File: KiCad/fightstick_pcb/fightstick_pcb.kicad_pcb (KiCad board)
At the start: 2 copper layers, 80.5 x 70 mm, 96 parts, among them J1 USB_B_Micro, J2 Conn_01x02, J3 Conn_01x02, J4 Screw_Terminal_01x12, J5 Screw_Terminal_01x12, J6 Screw_Terminal_01x12, SW1 SW_Push, U1 SN74LVC1G14DBV, U10 SN74LVC1G14DBV, U11 SN74LVC1G14DBV, U12 SN74LVC1G14DBV, U13 SN74LVC1G14DBV, U14 SN74LVC1G14DBV, U15 SN74LVC1G14DBV, U2 SN74LVC1G14DBV, U3 NCP1117-3.3_SOT223, U4 W25Q128JVS, U5 SN74LVC1G14DBV, U6 SN74LVC1G14DBV, U7 SN74LVC1G14DBV, U8 SN74LVC1G14DBV, U9 RP2040, Y1 ABM8-272-T3

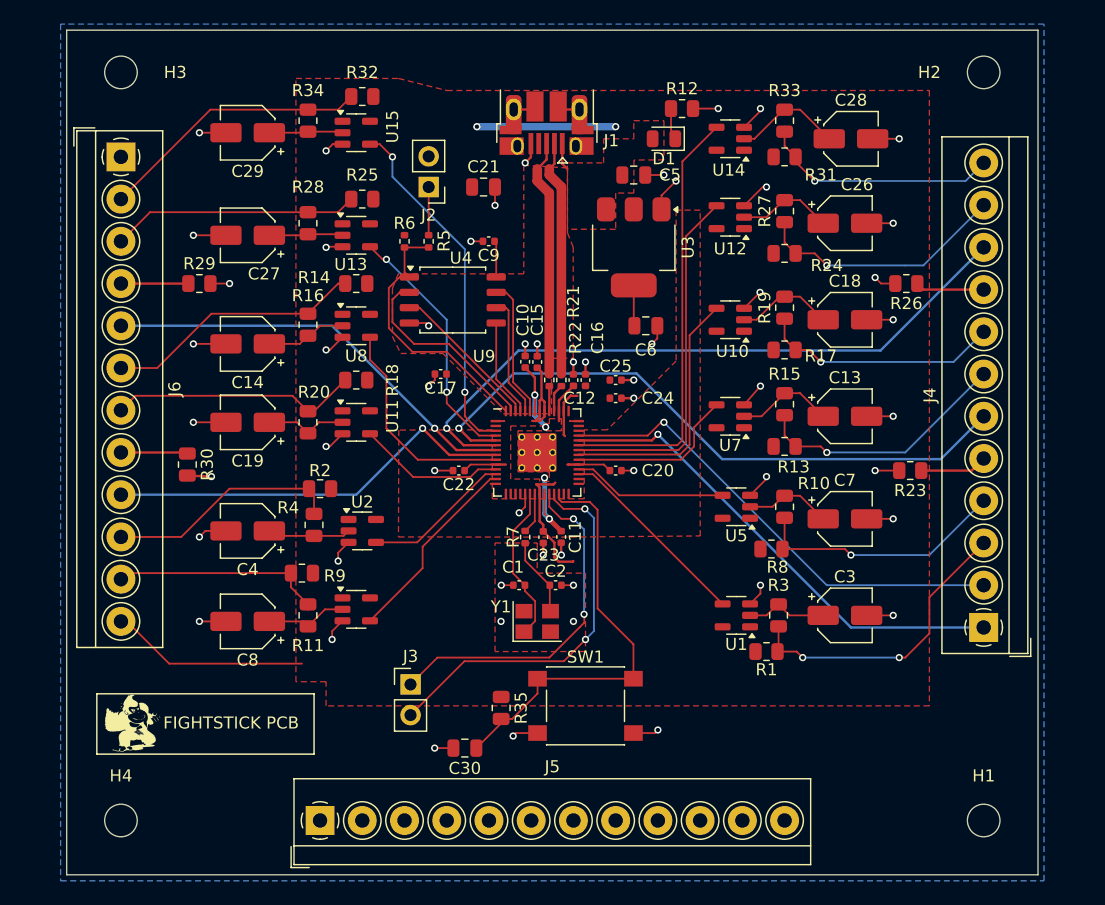
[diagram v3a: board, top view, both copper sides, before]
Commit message: PCB V1.1.0
Améliorations avec cap polarisés
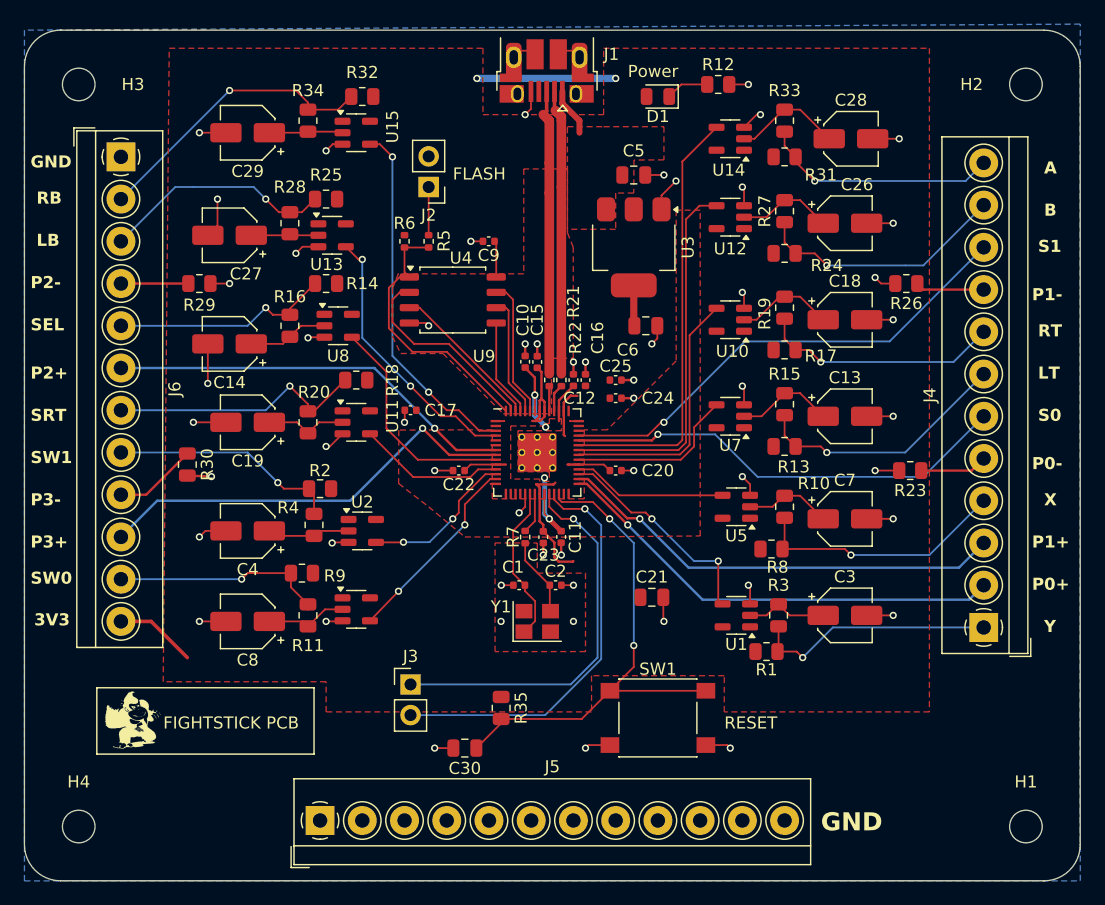
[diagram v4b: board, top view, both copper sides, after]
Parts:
- removed REF**: KiCad-Logo2_5mm_SilkScreen, Symbol:KiCad-Logo2_5mm_SilkScreen
- removed REF**: WEEE-Logo_4.2x6mm_SilkScreen, Symbol:WEEE-Logo_4.2x6mm_SilkScreen
- R12, R23, R26, R29, R30: value 1k -> 130
- R35: value 10k -> 1k
- moved C21 36.8 mm to (109.5, 112.0)
- moved SW1 6.08 mm to (110.0, 122.0)
- moved J1 4.33 mm to (100.8, 67.2)
- moved C17 3.91 mm to (89.5, 96.5)
- moved H2 3.64 mm to (140.5, 69.5)
- moved H3 3.64 mm to (62.0, 69.5)
- moved R12 3.61 mm to (115.0, 69.5)
- moved D1 3.54 mm to (110.0, 70.5)
- moved H1 3.54 mm to (140.5, 131.0)
- moved H4 3.54 mm to (62.0, 131.0)
- moved R25 3.00 mm to (82.5, 79.0)
- moved R14 2.50 mm to (82.5, 86.0)
- moved U13 2.00 mm to (83.0, 82.0)
- moved R16 1.50 mm to (79.5, 89.5)
- moved C14 1.50 mm to (74.5, 91.0)
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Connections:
- D1 pad 2: VBUS -> +3V3
- J4 pad 1: /SIG_STICK_0 -> /SW_Y
- J4 pad 10: /LED_P1+ -> /SIG_STICK_1
- J4 pad 2: /SIG_STICK_1 -> /LED_P0+
- J4 pad 3: /SW_Y -> /LED_P1+
- J4 pad 6: /LED_P0+ -> /SIG_STICK_0
- J6 pad 10: /SW_1 -> /LED_P3+
- J6 pad 5: /LED_P2+ -> /SW_SELECT
- J6 pad 6: /SW_SELECT -> /LED_P2+
- J6 pad 8: /LED_P3- -> /SW_1
- J6 pad 9: /LED_P3+ -> /LED_P3-
- U9 pad 29: unconnected-(U9-GPIO18-Pad29) -> /LED_P0+
- U9 pad 30: unconnected-(U9-GPIO19-Pad30) -> /LED_P1+
- U9 pad 5: /LED_P0+ -> unconnected-(U9-GPIO3-Pad5)
- U9 pad 6: /LED_P1+ -> unconnected-(U9-GPIO4-Pad6)
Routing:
- net /LED_P1+: track 55.6 -> 37.5 mm
- net /LED_P0+: track 53.3 -> 38.8 mm
- net +3V3: track 64.9 -> 55.7 mm
- net /RUN: track 35.6 -> 42.4 mm, vias 0 -> 2
- net /SW_Y: track 25.1 -> 20.5 mm, vias 2 -> 1
- net /USB_D+: track 19.8 -> 23.7 mm
- net /USB_D-: track 19.7 -> 23.5 mm
- net Net-(J3-Pin_1): track 29.0 -> 32.2 mm, vias 2 -> 1
- net /SW_SELECT: track 21.5 -> 18.3 mm, vias 0 -> 1
- net /SIG_STICK_0: track 40.4 -> 37.3 mm
- net GND: track 98.2 -> 95.8 mm
- net Net-(J3-Pin_2): track 32.4 -> 34.6 mm, vias 2 -> 1
- net /SIG_Y: track 16.4 -> 18.2 mm, vias 0 -> 2
- net /SIG_LB: track 21.0 -> 22.7 mm
- net VBUS: track 2.28 -> 4.01 mm
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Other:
- board size 80.5 x 70 mm -> 87.5 x 70.5 mm
- board text added: "3V3"
- board text added: "A"
- board text added: "B"
- board text added: "FLASH"
- board text added: "GND"
- board text added: "LB"
- board text added: "LT"
- board text added: "P0+"
- board text added: "P0-"
- board text added: "P1+"
- board text added: "P1-"
- board text added: "P2+"
- board text added: "P2-"
- board text added: "P3+"
- board text added: "P3-"
- board text added: "Power"
- board text added: "RB"
- board text added: "RESET"
- board text added: "RT"
- board text added: "S0"
- board text added: "S1"
- board text added: "SEL"
- board text added: "SRT"
- board text added: "SW0"
- board text added: "SW1"
- board text added: "X"
- board text added: "Y"

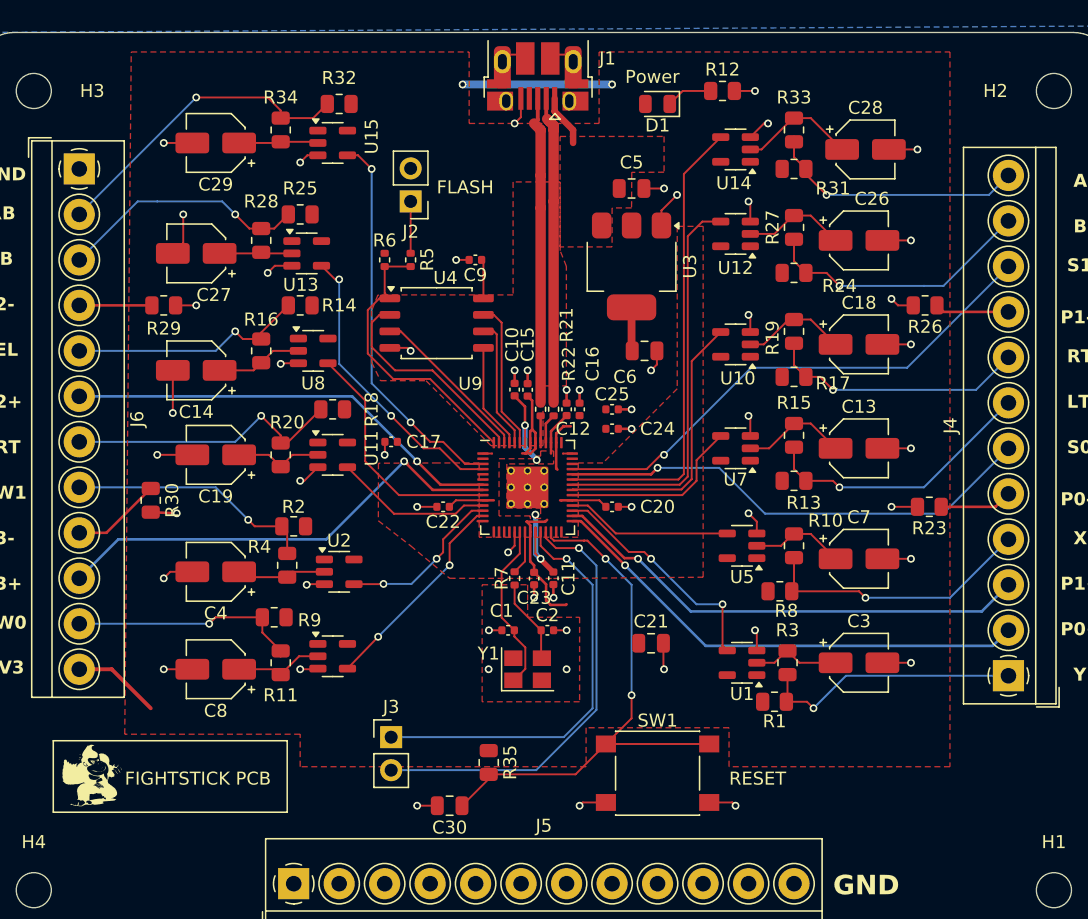
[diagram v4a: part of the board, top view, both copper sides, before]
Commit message: PCB V1.2
Il n'y a plus de condensateurs polarisés
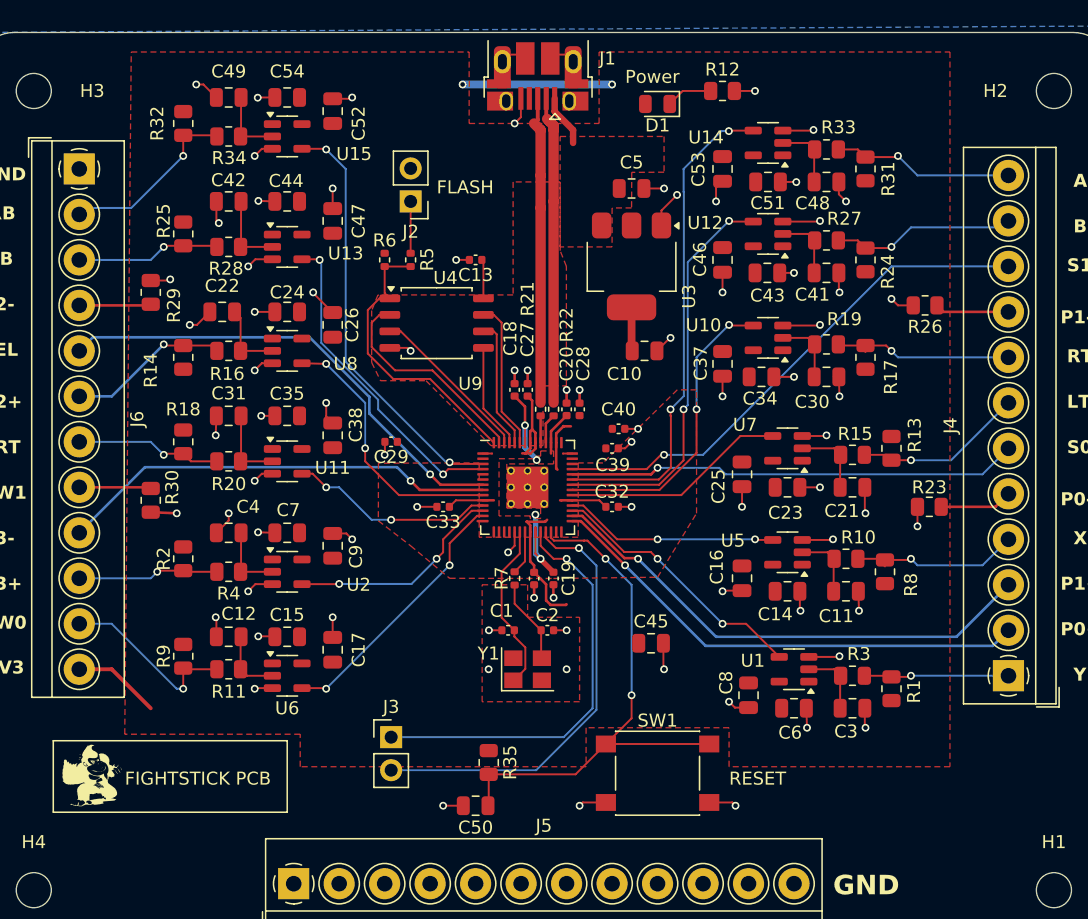
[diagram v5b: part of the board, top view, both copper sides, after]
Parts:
- added C31: 1u, Capacitor_SMD:C_0805_2012Metric, F.Cu at (77.0, 94.5)
- added C32: 100n, Capacitor_SMD:C_0402_1005Metric, F.Cu at (106.5, 101.5)
- added C33: 100n, Capacitor_SMD:C_0402_1005Metric, F.Cu at (93.5, 101.5)
- added C34: 0.1u, Capacitor_SMD:C_0805_2012Metric, F.Cu at (118.0, 91.5)
- added C35: 0.1u, Capacitor_SMD:C_0805_2012Metric, F.Cu at (81.5, 94.5)
- added C36: 100n, Capacitor_SMD:C_0402_1005Metric, F.Cu at (100.5, 107.0)
- added C37: 1u, Capacitor_SMD:C_0805_2012Metric, F.Cu at (115.0, 90.5)
- added C38: 1u, Capacitor_SMD:C_0805_2012Metric, F.Cu at (85.0, 96.0)
- added C39: 100n, Capacitor_SMD:C_0402_1005Metric, F.Cu at (106.5, 97.0)
- added C40: 100n, Capacitor_SMD:C_0402_1005Metric, F.Cu at (107.0, 95.5)
- added C41: 1u, Capacitor_SMD:C_0805_2012Metric, F.Cu at (123.0, 83.5)
- added C42: 1u, Capacitor_SMD:C_0805_2012Metric, F.Cu at (77.0, 78.0)
- added C43: 0.1u, Capacitor_SMD:C_0805_2012Metric, F.Cu at (118.5, 83.5)
- added C44: 0.1u, Capacitor_SMD:C_0805_2012Metric, F.Cu at (81.5, 78.0)
- added C45: 10u, Capacitor_SMD:C_0805_2012Metric, F.Cu at (109.5, 112.0)
- added C46: 1u, Capacitor_SMD:C_0805_2012Metric, F.Cu at (115.0, 82.5)
- added C47: 1u, Capacitor_SMD:C_0805_2012Metric, F.Cu at (85.0, 79.5)
- added C48: 1u, Capacitor_SMD:C_0805_2012Metric, F.Cu at (123.0, 76.5)
- added C49: 1u, Capacitor_SMD:C_0805_2012Metric, F.Cu at (77.0, 70.0)
- added C50: 100n, Capacitor_SMD:C_0805_2012Metric, F.Cu at (96.0, 124.5)
- added C51: 0.1u, Capacitor_SMD:C_0805_2012Metric, F.Cu at (118.5, 76.5)
- added C52: 0.1u, Capacitor_SMD:C_0805_2012Metric, F.Cu at (85.0, 71.0)
- added C53: 1u, Capacitor_SMD:C_0805_2012Metric, F.Cu at (115.0, 75.5)
- added C54: 1u, Capacitor_SMD:C_0805_2012Metric, F.Cu at (81.5, 70.0)
- C10: value 100n -> 10u; footprint Capacitor_SMD:C_0402_1005Metric -> Capacitor_SMD:C_0805_2012Metric
- C11, C17, C22, C25, C9: value 100n -> 1u; footprint Capacitor_SMD:C_0402_1005Metric -> Capacitor_SMD:C_0805_2012Metric
- C12, C16: footprint Capacitor_SMD:C_0402_1005Metric -> Capacitor_SMD:C_0805_2012Metric
- C13, C18, C19, C27, C29: value 1u -> 100n; footprint Capacitor_SMD:CP_Elec_4x3 -> Capacitor_SMD:C_0402_1005Metric
- C14, C7: value 1u -> 0.1u; footprint Capacitor_SMD:CP_Elec_4x3 -> Capacitor_SMD:C_0805_2012Metric
- C15, C23, C24: value 100n -> 0.1u; footprint Capacitor_SMD:C_0402_1005Metric -> Capacitor_SMD:C_0805_2012Metric
- C20, C30: value 100n -> 1u
- C21: value 10u -> 1u
- C26, C3, C4, C8: footprint Capacitor_SMD:CP_Elec_4x3 -> Capacitor_SMD:C_0805_2012Metric
- C28: footprint Capacitor_SMD:CP_Elec_4x3 -> Capacitor_SMD:C_0402_1005Metric
- C6: value 10u -> 0.1u
- moved C14 48.6 mm to (120.0, 108.0), turned to 0 degrees
- moved C7 44.0 mm to (81.5, 103.5), turned to 180 degrees
- moved C30 43.9 mm to (123.0, 91.5), turned to 0 degrees
- moved C8 41.0 mm to (117.0, 116.0), turned to -90 degrees
- moved C26 41.0 mm to (85.0, 87.5), turned to 90 degrees
- moved C13 32.9 mm to (96.0, 82.5), turned to 180 degrees
- moved C12 31.3 mm to (77.0, 111.5), turned to 180 degrees
- moved C6 29.8 mm to (120.5, 117.0)
- moved C28 29.7 mm to (104.0, 94.0), turned to 90 degrees
- moved C19 27.7 mm to (102.0, 107.0), turned to -90 degrees
- moved C27 27.6 mm to (100.0, 92.5), turned to 90 degrees
- moved C18 26.7 mm to (99.0, 92.5), turned to 90 degrees
- moved C29 26.7 mm to (89.5, 96.5)
- moved C24 26.6 mm to (81.5, 86.5), turned to 180 degrees
- moved C15 26.5 mm to (81.5, 111.5), turned to 180 degrees
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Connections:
- C10 pad 1: +1V1 -> +3V3
- C11 pad 1: +1V1 -> Net-(C11-Pad1)
- C12 pad 1: +1V1 -> Net-(C12-Pad1)
- C13 pad 1: Net-(C13-Pad1) -> +3V3
- C14 pad 1: Net-(C14-Pad1) -> +3V3
- C18 pad 1: Net-(C18-Pad1) -> +1V1
- C19 pad 1: Net-(C19-Pad1) -> +1V1
- C20 pad 1: +3V3 -> +1V1
- C21 pad 1: +3V3 -> Net-(C21-Pad1)
- C22 pad 1: +3V3 -> Net-(C22-Pad1)
- C26 pad 1: Net-(C26-Pad1) -> +3V3
- C27 pad 1: Net-(C27-Pad1) -> +3V3
- C28 pad 1: Net-(C28-Pad1) -> +3V3
- C29 pad 1: Net-(C29-Pad1) -> +3V3
- C30 pad 1: /RUN -> Net-(C30-Pad1)
- C7 pad 1: Net-(C7-Pad1) -> +3V3
- C8 pad 1: Net-(C8-Pad1) -> +3V3
- J6 pad 10: /LED_P3+ -> /SW_1
- J6 pad 5: /SW_SELECT -> /LED_P2+
- J6 pad 6: /LED_P2+ -> /SW_SELECT
- J6 pad 8: /SW_1 -> /LED_P3-
- J6 pad 9: /LED_P3- -> /LED_P3+
- R10 pad 2: Net-(C7-Pad1) -> Net-(C11-Pad1)
- R11 pad 2: Net-(C8-Pad1) -> Net-(C12-Pad1)
- R15 pad 2: Net-(C13-Pad1) -> Net-(C21-Pad1)
- R16 pad 2: Net-(C14-Pad1) -> Net-(C22-Pad1)
- R19 pad 2: Net-(C18-Pad1) -> Net-(C30-Pad1)
- R20 pad 2: Net-(C19-Pad1) -> Net-(C31-Pad1)
- R27 pad 2: Net-(C26-Pad1) -> Net-(C41-Pad1)
- R28 pad 2: Net-(C27-Pad1) -> Net-(C42-Pad1)
- R33 pad 2: Net-(C28-Pad1) -> Net-(C48-Pad1)
- R34 pad 2: Net-(C29-Pad1) -> Net-(C49-Pad1)
- U10 pad 2: Net-(C18-Pad1) -> Net-(C30-Pad1)
- U11 pad 2: Net-(C19-Pad1) -> Net-(C31-Pad1)
- U12 pad 2: Net-(C26-Pad1) -> Net-(C41-Pad1)
- U13 pad 2: Net-(C27-Pad1) -> Net-(C42-Pad1)
- U14 pad 2: Net-(C28-Pad1) -> Net-(C48-Pad1)
- U15 pad 2: Net-(C29-Pad1) -> Net-(C49-Pad1)
- U5 pad 2: Net-(C7-Pad1) -> Net-(C11-Pad1)
- U6 pad 2: Net-(C8-Pad1) -> Net-(C12-Pad1)
- U7 pad 2: Net-(C13-Pad1) -> Net-(C21-Pad1)
- U8 pad 2: Net-(C14-Pad1) -> Net-(C22-Pad1)
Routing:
- net GND: track 95.8 -> 129.4 mm, vias 55 -> 79
- net /SW_START: track 21.7 -> 11.3 mm
- net /SW_RB: track 24.3 -> 14.1 mm
- net /SW_Y: track 20.5 -> 11.3 mm
- net Net-(C28-Pad1): track 9.06 -> 0.00 mm
- net Net-(C18-Pad1): track 8.67 -> 0.00 mm
- net /SW_X: track 21.4 -> 12.8 mm
- net /SW_1: track 19.1 -> 10.9 mm
- net Net-(C13-Pad1): track 8.15 -> 0.00 mm
- net /SW_LT: track 21.5 -> 13.3 mm
- net Net-(C26-Pad1): track 7.94 -> 0.00 mm
- net /SW_LB: track 19.3 -> 11.6 mm
- net /SW_B: track 21.6 -> 14.2 mm
- net Net-(C7-Pad1): track 7.23 -> 0.00 mm
- net Net-(C8-Pad1): track 6.82 -> 0.00 mm
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
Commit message: PCB V1.2.1
Tous les condensateurs et résistances sont maintenant plus gros
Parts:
- C1, C13, C18, C19, C2, C20, C27, C28, C29, C32, C33, C36, C39, C40: footprint Capacitor_SMD:C_0402_1005Metric -> Capacitor_SMD:C_0805_2012Metric
- R21, R22, R5, R6, R7: footprint Resistor_SMD:R_0402_1005Metric -> Resistor_SMD:R_0805_2012Metric
- moved C13 7.52 mm to (95.5, 75.0)
- moved R5 5.10 mm to (92.0, 77.5)
- moved R6 5.00 mm to (89.0, 77.5)
- moved U4 4.86 mm to (93.0, 82.5)
- moved J2 4.72 mm to (91.0, 73.3)
- moved C18 4.47 mm to (97.0, 88.5)
- moved C27 4.12 mm to (99.0, 88.5)
- moved J3 3.00 mm to (86.5, 119.2)
- moved R21 2.11 mm to (99.5, 92.5)
- moved C28 1.80 mm to (105.5, 93.0)
- moved C40 1.80 mm to (108.5, 94.5)
- moved Y1 1.80 mm to (98.5, 115.0)
- moved R22 1.57 mm to (101.5, 92.5)
- moved C19 1.51 mm to (103.5, 107.0)
- moved C1 1.50 mm to (97.0, 111.0)
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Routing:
- net +3V3: track 55.7 -> 69.0 mm
- net /QSPI_SD3: track 11.5 -> 17.9 mm
- net /QSPI_SCLK: track 10.0 -> 16.4 mm
- net +1V1: track 17.7 -> 24.0 mm
- net /QSPI_SD0: track 8.12 -> 13.9 mm
- net /QSPI_SD2: track 12.7 -> 17.6 mm
- net Net-(J3-Pin_2): track 34.6 -> 38.5 mm
- net /QSPI_SS: track 22.8 -> 26.5 mm
- net Net-(J3-Pin_1): track 32.2 -> 35.7 mm
- net /QSPI_SD1: track 16.6 -> 19.5 mm
- net /XIN: track 13.2 -> 15.6 mm
- net /USB_D-: track 23.5 -> 21.5 mm
- net Net-(U9-USB_DP): track 2.06 -> 3.77 mm
- net /USB_D+: track 23.7 -> 22.0 mm
- net /SIG_START: track 15.9 -> 17.0 mm
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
